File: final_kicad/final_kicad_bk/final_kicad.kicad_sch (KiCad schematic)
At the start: 70 parts, among them J3 Reflectance Sensor Array, M1 Motor, M3 Servo for Side Indicator, M4 Servo for Gripper, M5 Motor_Step_4Wire, M6 Motor for Linear Actuator, Q1 Photo_NPN, Q2 MOSFET-N, SW1 Reset, SW2 Reset, U0 PIC32MX170F256B, U1 SN754410, U2 MCP6294, U2 PIC32MX170F256B, U4 Comparator, U5 L293NE, U6 L293NE

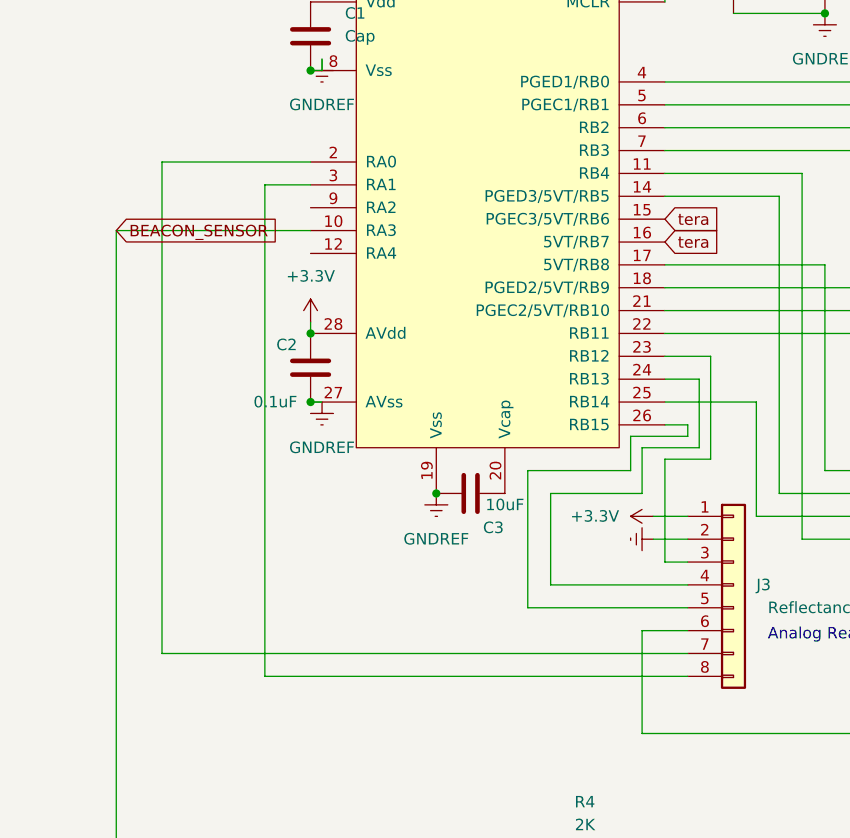
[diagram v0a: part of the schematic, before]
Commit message: analog reading all work
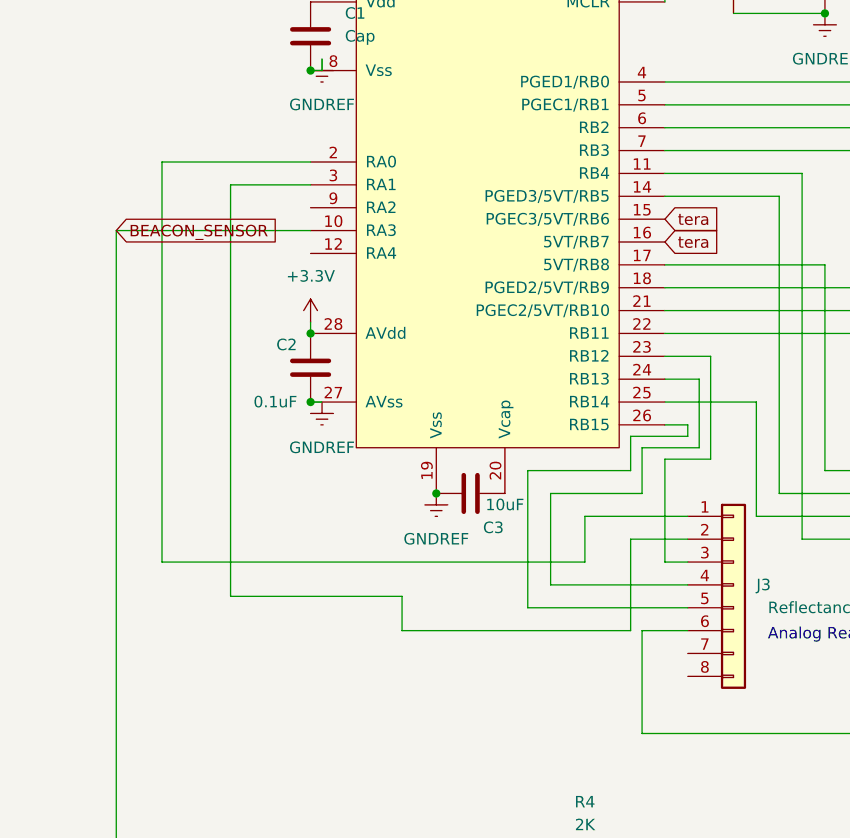
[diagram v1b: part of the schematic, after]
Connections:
- net +3.3V: no longer J3.1 (Pin_1)
- net Earth: no longer J3.2 (Pin_2)
- net at U2.2 (RA0): now also J3.1 (Pin_1); no longer J3.7 (Pin_7)
- net at U2.3 (RA1): now also J3.2 (Pin_2); no longer J3.8 (Pin_8)
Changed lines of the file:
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@@
     (stroke (width 0) (type default))
   )
-  (wire (pts (xy 62.23 148.59) (xy 109.22 148.59))
-    (stroke (width 0) (type default))
-  )
   (wire (pts (xy 257.81 302.26) (xy 248.92 302.26))
     (stroke (width 0) (type default))
@@
     (stroke (width 0) (type default))
   )
+  (wire (pts (xy 58.42 93.98) (xy 58.42 139.7))
+    (stroke (width 0) (type default))
+  )
   (wire (pts (xy 95.25 328.93) (xy 95.25 331.47))
     (stroke (width 0) (type default))
@@
     (stroke (width 0) (type default))
   )
-  (wire (pts (xy 50.8 91.44) (xy 50.8 146.05))
-    (stroke (width 0) (type default))
-  )
   (wire (pts (xy 139.7 186.69) (xy 139.7 189.23))
     (stroke (width 0) (type default))
@@
     (stroke (width 0) (type default))
   )
+  (wire (pts (xy 97.79 135.89) (xy 97.79 130.81))
+    (stroke (width 0) (type default))
+  )
   (wire (pts (xy 190.5 278.13) (xy 194.31 278.13))
     (stroke (width 0) (type default))
@@
     (stroke (width 0) (type default))
   )
+  (wire (pts (xy 58.42 139.7) (xy 77.47 139.7))
+    (stroke (width 0) (type default))
+  )
   (wire (pts (xy 309.88 97.79) (xy 309.88 105.41))
     (stroke (width 0) (type default))
@@
     (stroke (width 0) (type default))
   )
-  (wire (pts (xy 109.22 130.81) (xy 105.41 130.81))
-    (stroke (width 0) (type default))
-  )
   (wire (pts (xy 267.97 302.26) (xy 267.97 297.18))
     (stroke (width 0) (type default))
@@
     (stroke (width 0) (type default))
   )
-  (wire (pts (xy 109.22 133.35) (xy 105.41 133.35))
-    (stroke (width 0) (type default))
-  )
   (wire (pts (xy 182.88 283.21) (xy 198.12 283.21))
     (stroke (width 0) (type default))
@@
     (stroke (width 0) (type default))
   )
+  (wire (pts (xy 77.47 139.7) (xy 77.47 143.51))
+    (stroke (width 0) (type default))
+  )
   (wire (pts (xy 233.68 64.77) (xy 233.68 87.63))
     (stroke (width 0) (type default))
@@
     (stroke (width 0) (type default))
   )
+  (wire (pts (xy 97.79 130.81) (xy 109.22 130.81))
+    (stroke (width 0) (type default))
+  )
   (wire (pts (xy 76.2 307.34) (xy 76.2 306.07))
     (stroke (width 0) (type default))
@@
     (stroke (width 0) (type default))
   )
+  (wire (pts (xy 102.87 133.35) (xy 109.22 133.35))
+    (stroke (width 0) (type default))
+  )
   (wire (pts (xy 106.68 120.65) (xy 109.22 120.65))
     (stroke (width 0) (type default))
@@
     (stroke (width 0) (type default))
   )
-  (wire (pts (xy 50.8 146.05) (xy 109.22 146.05))
-    (stroke (width 0) (type default))
-  )
   (wire (pts (xy 210.82 97.79) (xy 241.3 97.79))
     (stroke (width 0) (type default))
@@
     (stroke (width 0) (type default))
   )
+  (wire (pts (xy 102.87 143.51) (xy 102.87 133.35))
+    (stroke (width 0) (type default))
+  )
+  (wire (pts (xy 50.8 135.89) (xy 97.79 135.89))
+    (stroke (width 0) (type default))
+  )
   (wire (pts (xy 226.06 254) (xy 226.06 274.32))
     (stroke (width 0) (type default))
@@
     (stroke (width 0) (type default))
   )
+  (wire (pts (xy 77.47 143.51) (xy 102.87 143.51))
+    (stroke (width 0) (type default))
+  )
   (wire (pts (xy 241.3 298.45) (xy 246.38 298.45))
     (stroke (width 0) (type default))
@@
     (stroke (width 0) (type default))
   )
-  (wire (pts (xy 67.31 93.98) (xy 62.23 93.98))
+  (wire (pts (xy 58.42 93.98) (xy 67.31 93.98))
     (stroke (width 0) (type default))
   )
@@
     (stroke (width 0) (type default))
   )
-  (wire (pts (xy 62.23 93.98) (xy 62.23 148.59))
-    (stroke (width 0) (type default))
-  )
   (wire (pts (xy 194.31 293.37) (xy 194.31 278.13))
     (stroke (width 0) (type default))
@@
     (stroke (width 0) (type default))
   )
+  (wire (pts (xy 50.8 91.44) (xy 50.8 135.89))
+    (stroke (width 0) (type default))
+  )
   (wire (pts (xy 246.38 267.97) (xy 257.81 267.97))
     (stroke (width 0) (type default))
@@
       (effects (font (size 1.27 1.27)) hide)
     )
-    (pin "3")
     (pin "1")
     (pin "2")
+    (pin "3")
     (instances
       (project "final_kicad"
@@
     )
   )
-  (symbol (lib_id "power:+3.3V") (at 105.41 130.81 90) (unit 1)
-    (in_bom yes) (on_board yes) (dnp no) (fields_autoplaced)
-    (property "Reference" "#PWR018" (at 109.22 130.81 0)
-      (effects (font (size 1.27 1.27)) hide)
-    )
-    (property "Value" "+3.3V" (at 101.6 130.81 90)
-      (effects (font (size 1.27 1.27)) (justify left))
-    )
-    (property "Footprint" "" (at 105.41 130.81 0)
-      (effects (font (size 1.27 1.27)) hide)
-    )
-    (property "Datasheet" "" (at 105.41 130.81 0)
-      (effects (font (size 1.27 1.27)) hide)
-    )
-    (pin "1")
-    (instances
-      (project "final_kicad"
-        (path "/dd0cc16c-02d9-42f4-90a9-b5b59b4b5d24"
-          (reference "#PWR018") (unit 1)
-        )
-      )
-    )
-  )
   (symbol (lib_id "ME218_BaseLib:LED") (at 48.26 311.15 0) (unit 1)
     (in_bom yes) (on_board yes) (dnp no)
@@
       (effects (font (size 1.27 1.27)) hide)
     )
-    (pin "3")
     (pin "1")
     (pin "2")
+    (pin "3")
     (instances
       (project "final_kicad"
@@
       (effects (font (size 1.27 1.27)) hide)
     )
-    (pin "8")
+    (pin "1")
+    (pin "2")
+    (pin "3")
     (pin "4")
     (pin "5")
     (pin "6")
     (pin "7")
-    (pin "3")
-    (pin "1")
-    (pin "2")
+    (pin "8")
     (instances
       (project "final_kicad"
@@
     )
     (pin "1")
-    (pin "3")
     (pin "2")
+    (pin "3")
     (instances
       (project "final_kicad"
@@
         )
       )
-    )
-  )
-  (symbol (lib_id "power:Earth") (at 105.41 133.35 270) (unit 1)
-    (in_bom yes) (on_board yes) (dnp no) (fields_autoplaced)
-    (property "Reference" "#PWR019" (at 99.06 133.35 0)
-      (effects (font (size 1.27 1.27)) hide)
-    )
-    (property "Value" "Earth" (at 101.6 133.35 0)
-      (effects (font (size 1.27 1.27)) hide)
-    )
-    (property "Footprint" "" (at 105.41 133.35 0)
-      (effects (font (size 1.27 1.27)) hide)
-    )
-    (property "Datasheet" "~" (at 105.41 133.35 0)
-      (effects (font (size 1.27 1.27)) hide)
-    )
-    (pin "1")
-    (instances
-      (project "final_kicad"
-        (path "/dd0cc16c-02d9-42f4-90a9-b5b59b4b5d24"
-          (reference "#PWR019") (unit 1)
-        )
-      )

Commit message: fix kicad
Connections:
- net MISO/SDI: now also U0.24 (RB13); no longer U0.14 (PGED3/5VT/RB5)
- net at M4.1 (PWM): now also U0.14 (PGED3/5VT/RB5); no longer U0.24 (RB13)
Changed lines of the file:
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@@
+    (stroke (width 0) (type default))
+  )
+  (wire (pts (xy 135.89 278.13) (xy 139.7 278.13))
     (stroke (width 0) (type default))
   )
@@
     (stroke (width 0) (type default))
   )
-  (wire (pts (xy 146.05 297.18) (xy 157.48 297.18))
-    (stroke (width 0) (type default))
-  )
   (wire (pts (xy 106.68 82.55) (xy 142.24 82.55))
     (stroke (width 0) (type default))
@@
     (stroke (width 0) (type default))
   )
-  (wire (pts (xy 142.24 316.23) (xy 142.24 311.15))
-    (stroke (width 0) (type default))
-  )
   (wire (pts (xy 236.22 265.43) (xy 236.22 283.21))
     (stroke (width 0) (type default))
@@
     (stroke (width 0) (type default))
   )
+  (wire (pts (xy 139.7 316.23) (xy 142.24 316.23))
+    (stroke (width 0) (type default))
+  )
   (wire (pts (xy 267.97 297.18) (xy 269.24 297.18))
     (stroke (width 0) (type default))
@@
     (stroke (width 0) (type default))
   )
-  (wire (pts (xy 140.97 311.15) (xy 142.24 311.15))
-    (stroke (width 0) (type default))
-  )
   (wire (pts (xy 54.61 317.5) (xy 54.61 311.15))
     (stroke (width 0) (type default))
@@
     (stroke (width 0) (type default))
   )
-  (wire (pts (xy 135.89 278.13) (xy 146.05 278.13))
-    (stroke (width 0) (type default))
-  )
   (wire (pts (xy 135.89 267.97) (xy 166.37 267.97))
     (stroke (width 0) (type default))
@@
     (stroke (width 0) (type default))
   )
+  (wire (pts (xy 139.7 278.13) (xy 139.7 316.23))
+    (stroke (width 0) (type default))
+  )
   (wire (pts (xy 267.97 302.26) (xy 267.97 297.18))
     (stroke (width 0) (type default))
@@
     (stroke (width 0) (type default))
   )
-  (wire (pts (xy 140.97 298.45) (xy 140.97 311.15))
-    (stroke (width 0) (type default))
-  )
   (wire (pts (xy 241.3 64.77) (xy 241.3 97.79))
     (stroke (width 0) (type default))
@@
     (stroke (width 0) (type default))
   )
-  (wire (pts (xy 146.05 278.13) (xy 146.05 297.18))
-    (stroke (width 0) (type default))
-  )
   (wire (pts (xy 241.3 273.05) (xy 262.89 273.05))
     (stroke (width 0) (type default))
@@
     (stroke (width 0) (type default))
   )
+  (wire (pts (xy 157.48 297.18) (xy 140.97 297.18))
+    (stroke (width 0) (type default))
+  )
   (wire (pts (xy 40.64 317.5) (xy 40.64 311.15))
     (stroke (width 0) (type default))
@@
     (stroke (width 0) (type default))
   )
+  (wire (pts (xy 140.97 297.18) (xy 140.97 298.45))
+    (stroke (width 0) (type default))
+  )
